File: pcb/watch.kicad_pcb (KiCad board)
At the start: 4 copper layers, 38 x 42.5 mm, 78 parts, among them J1 Conn_01x04_Female, J2 Batt, J3 Conn_01x04_Female, Q1 AO3401A, Q10 VBK162K, Q11 VBK162K, Q2 VBK162K, Q3 VBK162K, Q4 VBK162K, Q5 VBK162K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

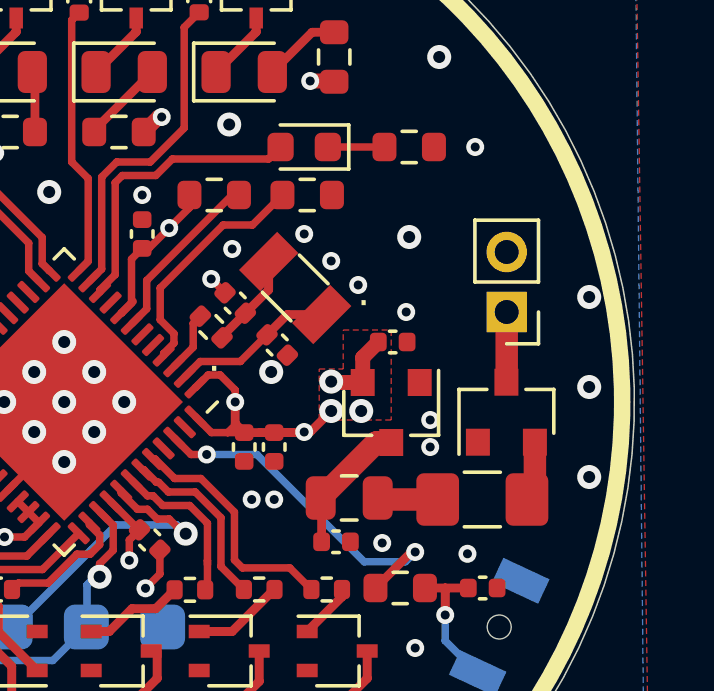
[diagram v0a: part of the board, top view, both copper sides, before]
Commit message: PCB - fix reverse polarity protection with a diode
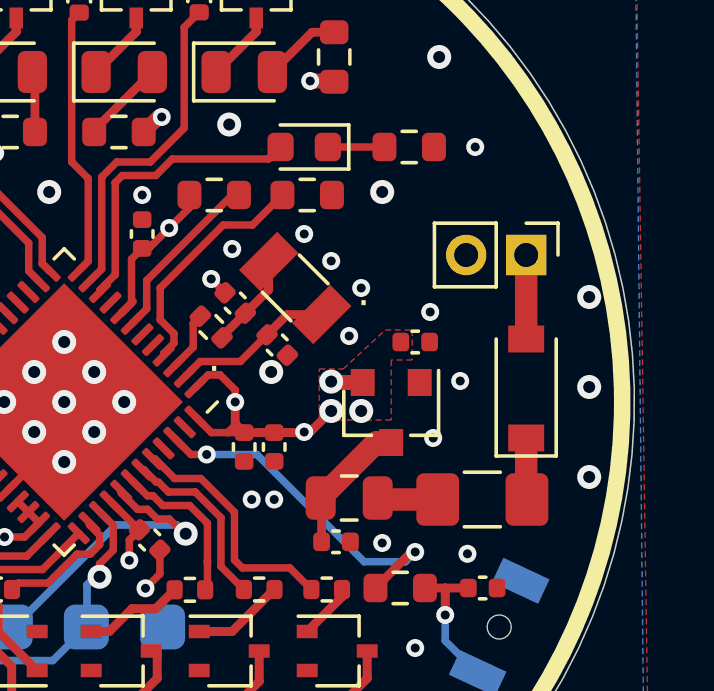
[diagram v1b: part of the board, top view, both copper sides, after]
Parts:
- removed Q1: AO3401A, Package_TO_SOT_SMD:SOT-23
- added D12: B5819W, Diode_SMD:D_SOD-123, F.Cu at (45.9, 30.1)
- moved J2 2.01 mm to (45.9, 25.6), turned to 270 degrees
- moved C10 0.75 mm to (42.2, 28.5)
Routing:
- net VDD: track 61.4 -> 59.8 mm
- net GND: vias 87 -> 88
